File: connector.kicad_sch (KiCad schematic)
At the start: 4 parts, among them J1 Conn_01x04_Pin, J2 Conn_01x04_Pin, J3 Conn_01x09_Pin, J4 Conn_02x03_Odd_Even

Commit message: added footprints to all the symbol
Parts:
- J1, J2: footprint (none) -> Connector_PinHeader_2.54mm:PinHeader_1x04_P2.54mm_Vertical
- J3: footprint (none) -> Connector_PinHeader_2.54mm:PinHeader_1x09_P2.54mm_Vertical
- J4: footprint (none) -> Connector_PinHeader_2.54mm:PinHeader_2x03_P2.54mm_Vertical
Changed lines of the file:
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@@
       (effects (font (size 1.27 1.27)))
     )
-    (property "Footprint" "" (at 111.76 82.55 0)
+    (property "Footprint" "Connector_PinHeader_2.54mm:PinHeader_2x03_P2.54mm_Vertical" (at 111.76 82.55 0)
       (effects (font (size 1.27 1.27)) hide)
     )
@@
       (effects (font (size 1.27 1.27)))
     )
-    (property "Footprint" "" (at 87.63 60.96 0)
+    (property "Footprint" "Connector_PinHeader_2.54mm:PinHeader_1x04_P2.54mm_Vertical" (at 87.63 60.96 0)
       (effects (font (size 1.27 1.27)) hide)
     )
@@
       (effects (font (size 1.27 1.27)))
     )
-    (property "Footprint" "" (at 81.28 87.63 0)
+    (property "Footprint" "Connector_PinHeader_2.54mm:PinHeader_1x09_P2.54mm_Vertical" (at 81.28 87.63 0)
       (effects (font (size 1.27 1.27)) hide)
     )
@@
       (effects (font (size 1.27 1.27)))
     )
-    (property "Footprint" "" (at 111.76 60.96 0)
+    (property "Footprint" "Connector_PinHeader_2.54mm:PinHeader_1x04_P2.54mm_Vertical" (at 111.76 60.96 0)
       (effects (font (size 1.27 1.27)) hide)
     )

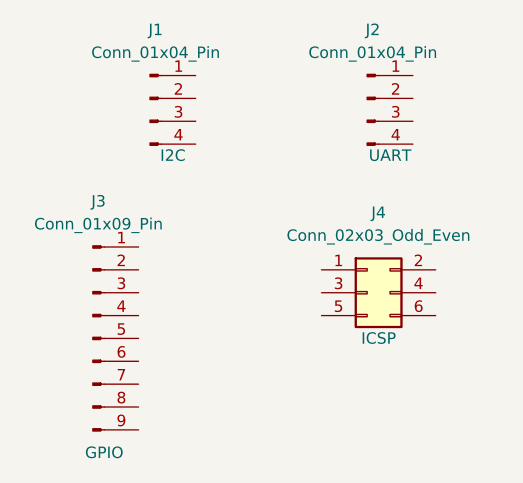
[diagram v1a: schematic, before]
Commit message: Completed wiring of sheet 2
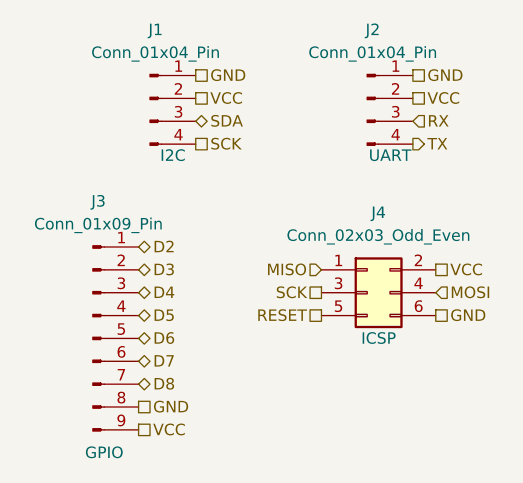
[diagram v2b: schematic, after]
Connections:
- net MISO: now reaches J4.1 (Pin_1)
- net VCC: now reaches J4.2 (Pin_2)
- net VCC: now also J1.2 (Pin_2), J2.2 (Pin_2), J3.9 (Pin_9)
- net SCK: now reaches J4.3 (Pin_3)
- net SCK: now also J1.4 (Pin_4)
- net MOSI: now reaches J4.4 (Pin_4)
- net RESET: now reaches J4.5 (Pin_5)
- net GND: now reaches J4.6 (Pin_6)
- net GND: now also J1.1 (Pin_1), J2.1 (Pin_1), J3.8 (Pin_8)
- net SDA: now reaches J1.3 (Pin_3)
- net D2: now reaches J3.1 (Pin_1)
- net D3: now reaches J3.2 (Pin_2)
- net D4: now reaches J3.3 (Pin_3)
- net D5: now reaches J3.4 (Pin_4)
- net D6: now reaches J3.5 (Pin_5)
- net D7: now reaches J3.6 (Pin_6)
- net D8: now reaches J3.7 (Pin_7)
- net RX: now reaches J2.3 (Pin_3)
- net TX: now reaches J2.4 (Pin_4)
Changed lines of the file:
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@@
 (kicad_sch (version 20230121) (generator eeschema)
   (paper "A4")
+  (hierarchical_label "VCC" (shape passive) (at 119.38 80.01 0) (fields_autoplaced)
+    (effects (font (size 1.27 1.27)) (justify left))
+  )
+  (hierarchical_label "MISO" (shape input) (at 106.68 80.01 180) (fields_autoplaced)
+    (effects (font (size 1.27 1.27)) (justify right))
+  )
+  (hierarchical_label "SCK" (shape passive) (at 106.68 82.55 180) (fields_autoplaced)
+    (effects (font (size 1.27 1.27)) (justify right))
+  )
+  (hierarchical_label "D7" (shape bidirectional) (at 86.36 90.17 0) (fields_autoplaced)
+    (effects (font (size 1.27 1.27)) (justify left))
+  )
+  (hierarchical_label "VCC" (shape passive) (at 116.84 60.96 0) (fields_autoplaced)
+    (effects (font (size 1.27 1.27)) (justify left))
+  )
+  (hierarchical_label "D2" (shape bidirectional) (at 86.36 77.47 0) (fields_autoplaced)
+    (effects (font (size 1.27 1.27)) (justify left))
+  )
+  (hierarchical_label "VCC" (shape passive) (at 92.71 60.96 0) (fields_autoplaced)
+    (effects (font (size 1.27 1.27)) (justify left))
+  )
+  (hierarchical_label "D4" (shape bidirectional) (at 86.36 82.55 0) (fields_autoplaced)
+    (effects (font (size 1.27 1.27)) (justify left))
+  )
+  (hierarchical_label "D6" (shape bidirectional) (at 86.36 87.63 0) (fields_autoplaced)
+    (effects (font (size 1.27 1.27)) (justify left))
+  )
+  (hierarchical_label "GND" (shape passive) (at 86.36 95.25 0) (fields_autoplaced)
+    (effects (font (size 1.27 1.27)) (justify left))
+  )
+  (hierarchical_label "GND" (shape passive) (at 92.71 58.42 0) (fields_autoplaced)
+    (effects (font (size 1.27 1.27)) (justify left))
+  )
+  (hierarchical_label "RX" (shape input) (at 116.84 63.5 0) (fields_autoplaced)
+    (effects (font (size 1.27 1.27)) (justify left))
+  )
+  (hierarchical_label "SCK" (shape passive) (at 92.71 66.04 0) (fields_autoplaced)
+    (effects (font (size 1.27 1.27)) (justify left))
+  )
+  (hierarchical_label "VCC" (shape passive) (at 86.36 97.79 0) (fields_autoplaced)
+    (effects (font (size 1.27 1.27)) (justify left))
+  )
+  (hierarchical_label "TX" (shape output) (at 116.84 66.04 0) (fields_autoplaced)
+    (effects (font (size 1.27 1.27)) (justify left))
+  )
+  (hierarchical_label "GND" (shape passive) (at 119.38 85.09 0) (fields_autoplaced)
+    (effects (font (size 1.27 1.27)) (justify left))
+  )
+  (hierarchical_label "SDA" (shape bidirectional) (at 92.71 63.5 0) (fields_autoplaced)
+    (effects (font (size 1.27 1.27)) (justify left))
+  )
+  (hierarchical_label "D8" (shape bidirectional) (at 86.36 92.71 0) (fields_autoplaced)
+    (effects (font (size 1.27 1.27)) (justify left))
+  )
+  (hierarchical_label "GND" (shape passive) (at 116.84 58.42 0) (fields_autoplaced)
+    (effects (font (size 1.27 1.27)) (justify left))
+  )
+  (hierarchical_label "MOSI" (shape input) (at 119.38 82.55 0) (fields_autoplaced)
+    (effects (font (size 1.27 1.27)) (justify left))
+  )
+  (hierarchical_label "RESET" (shape passive) (at 106.68 85.09 180) (fields_autoplaced)
+    (effects (font (size 1.27 1.27)) (justify right))
+  )
+  (hierarchical_label "D3" (shape bidirectional) (at 86.36 80.01 0) (fields_autoplaced)
+    (effects (font (size 1.27 1.27)) (justify left))
+  )
+  (hierarchical_label "D5" (shape bidirectional) (at 86.36 85.09 0) (fields_autoplaced)
+    (effects (font (size 1.27 1.27)) (justify left))
+  )
   (symbol (lib_id "Connector_Generic:Conn_02x03_Odd_Even") (at 111.76 82.55 0) (unit 1)
     (in_bom yes) (on_board yes) (dnp no)

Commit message: 2 detects are resolved in schematic
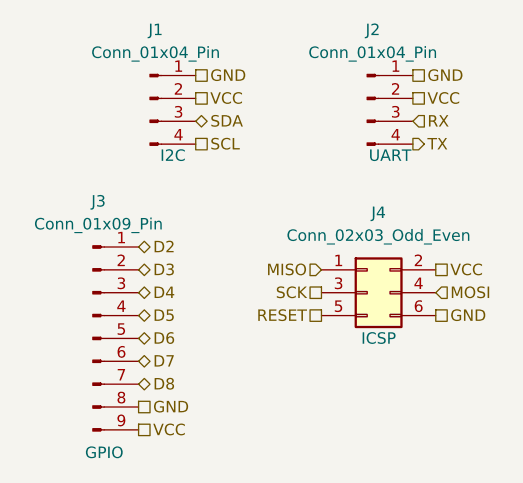
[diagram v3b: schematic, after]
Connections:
- net SCK: no longer J1.4 (Pin_4)
- new net SCL: J1.4 (Pin_4)
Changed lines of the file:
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@@
     (effects (font (size 1.27 1.27)) (justify left))
   )
-  (hierarchical_label "SCK" (shape passive) (at 92.71 66.04 0) (fields_autoplaced)
+  (hierarchical_label "SCL" (shape passive) (at 92.71 66.04 0) (fields_autoplaced)
     (effects (font (size 1.27 1.27)) (justify left))
   )
